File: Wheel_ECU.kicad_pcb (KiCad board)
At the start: 2 copper layers, 61 x 61 mm, 64 parts, among them J1 Conn_01x04, J2 Conn_01x04, J3 Conn_01x02, J4 Debug, J5 Conn_01x02, U1 IFX9201SG, U2 TLE4964, U3 XMC1404_F064, U4 TLE7251, U5 LM35-D

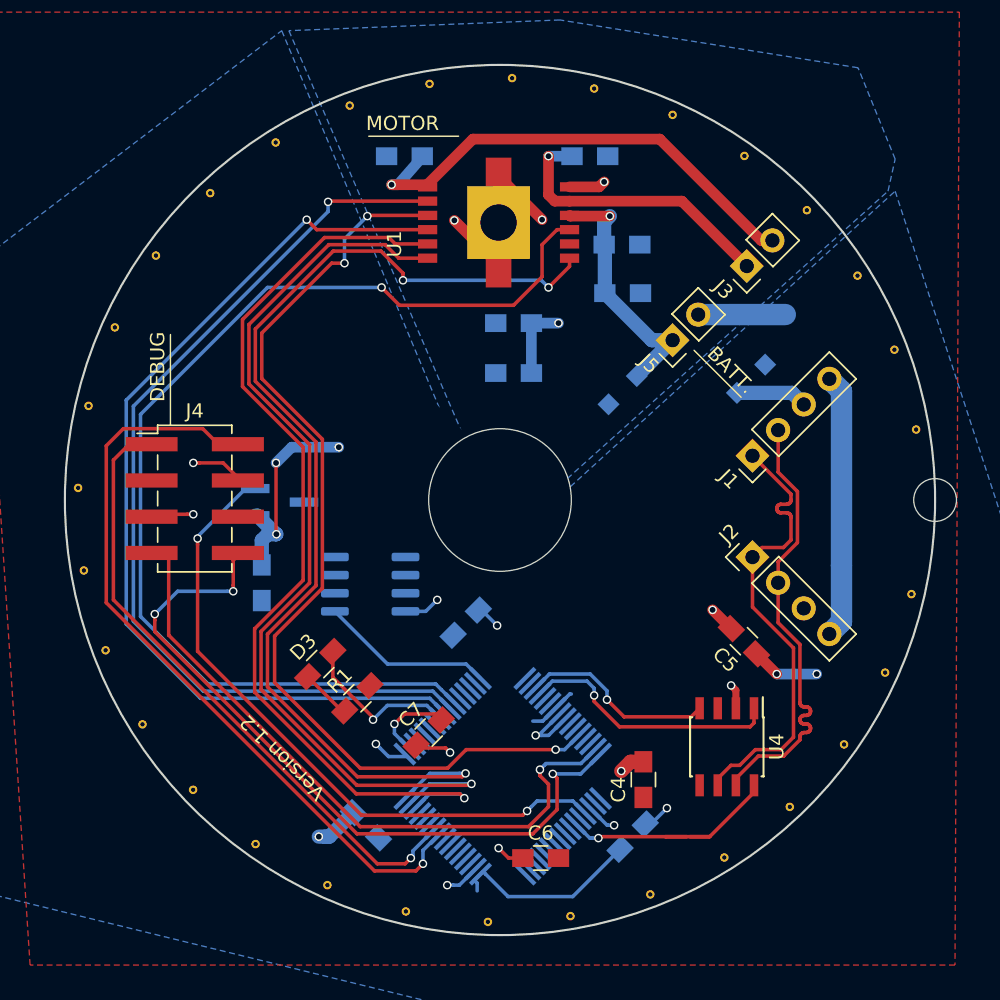
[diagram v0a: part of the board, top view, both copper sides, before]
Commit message: Fix silk screen and texts and smaller improvements
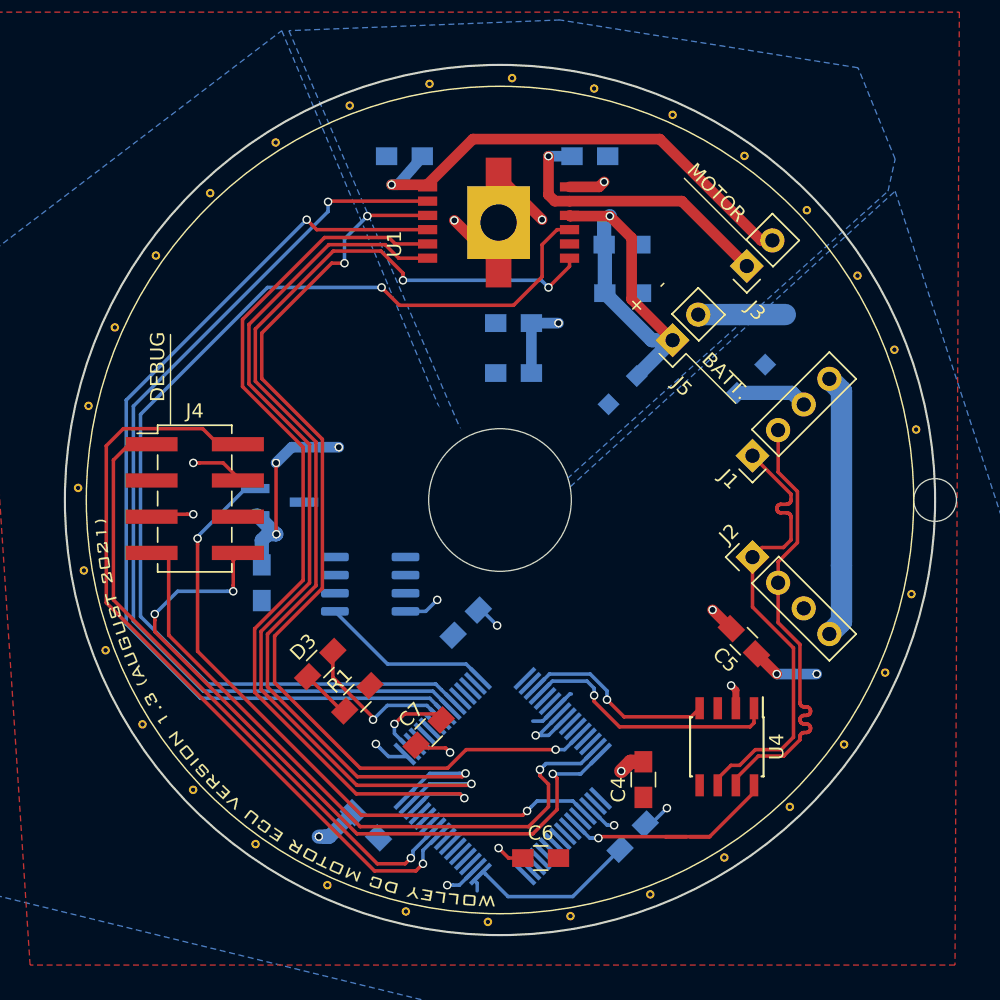
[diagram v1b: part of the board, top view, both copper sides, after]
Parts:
- added G***: LOGO, WheelECU:Text_Wolley_DC_Motor_ECU_SilkScreen, F.Cu at (117.4, 113.3)
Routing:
- net +BATT: track 18.1 -> 28.6 mm
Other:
- board text added: "+"
- board text added: "-"
- board text removed: "Version 1.2"

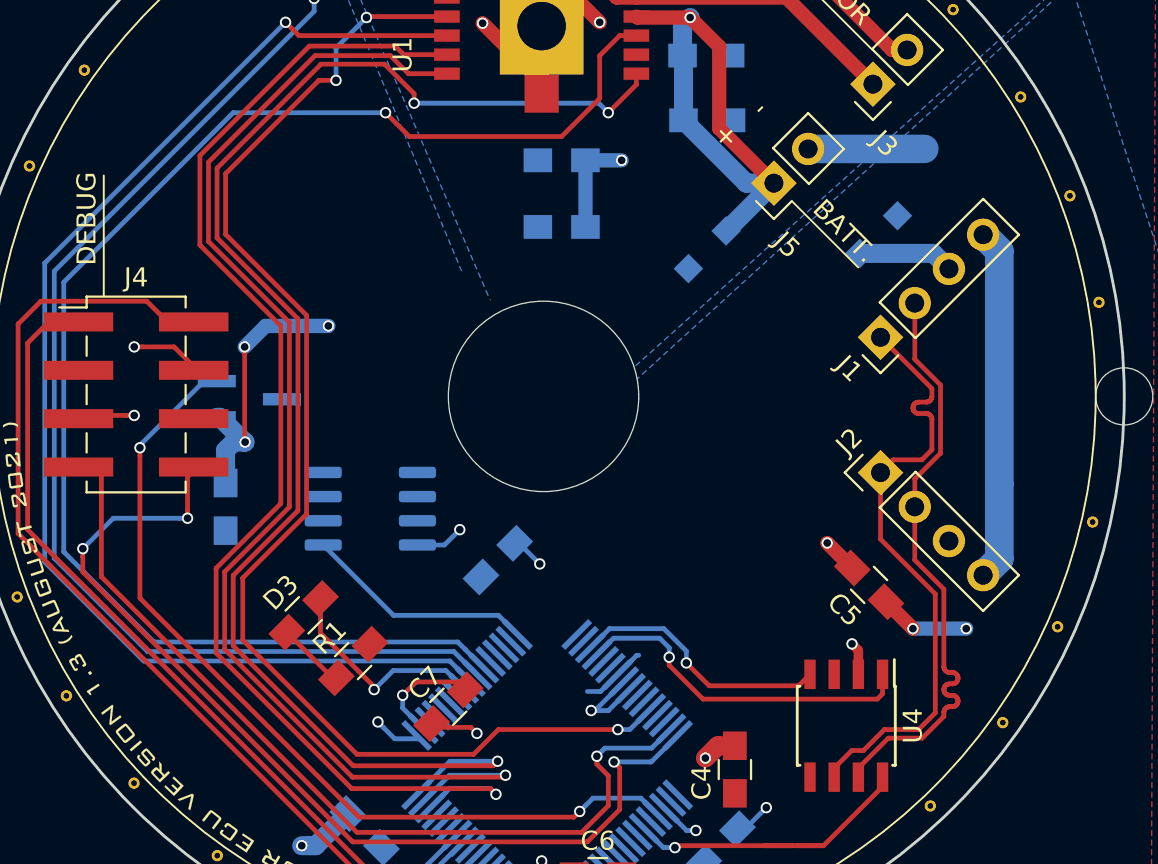
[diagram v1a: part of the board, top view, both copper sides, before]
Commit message: Relocate the second connector a bit and add mor space between the labels
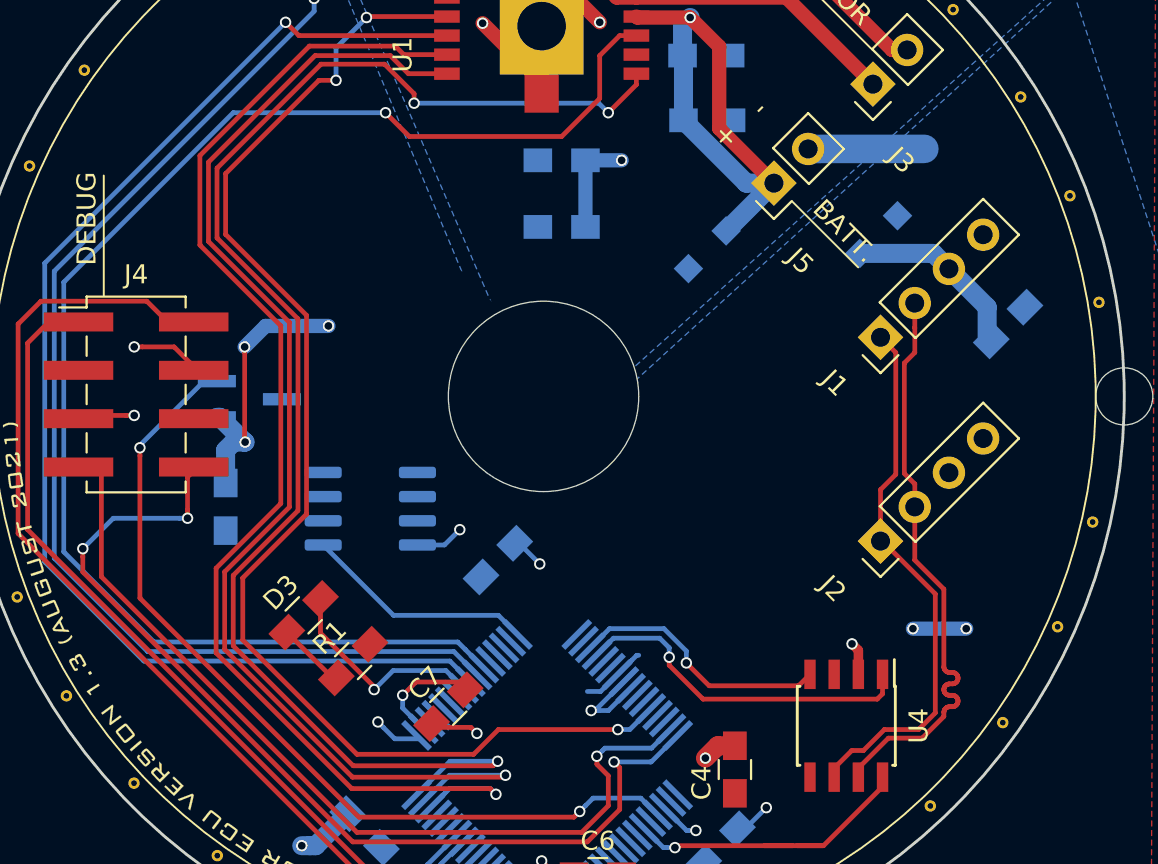
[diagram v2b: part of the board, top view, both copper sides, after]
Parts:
- C5: moved to B.Cu
- moved C5 15.5 mm to (156.2, 94.6), turned to 45 degrees
- moved J2 3.60 mm to (149.5, 106.0), turned to 135 degrees
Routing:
- net GND: track 80.2 -> 59.8 mm, vias 11 -> 10
- net CAN-: track 32.5 -> 28.7 mm
- net +5V: track 55.9 -> 58.4 mm
- net CAN+: track 31.5 -> 30.8 mm
